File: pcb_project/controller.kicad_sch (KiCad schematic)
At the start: 16 parts, among them U5 COM-09032, U6 COM-09032

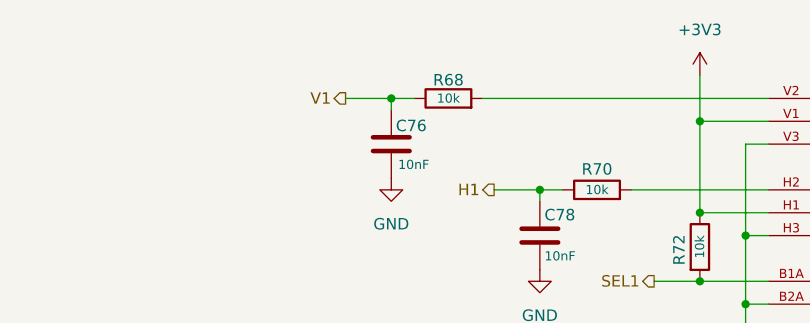
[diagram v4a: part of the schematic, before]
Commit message: Fix USB pins and other ERC errors
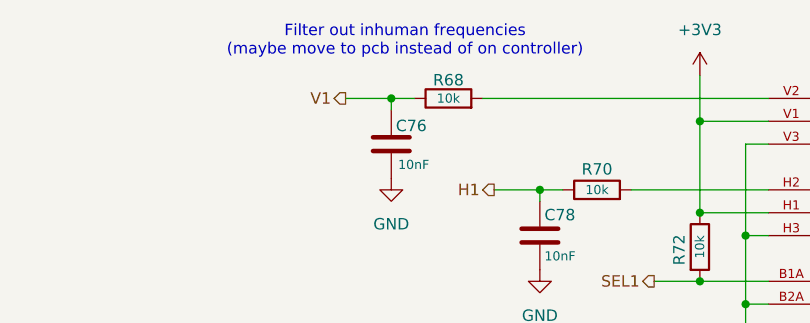
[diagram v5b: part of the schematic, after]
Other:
- note added: "Filter out inhuman frequencies (maybe move to pcb instead of on controller)"
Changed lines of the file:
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@@
 	(generator_version "9.0")
 	(paper "A4")
+	(text "Filter out inhuman frequencies \n(maybe move to pcb instead of on controller)"
+		(exclude_from_sim no)
+		(at 156.464 34.29 0)
+		(effects
+			(font
+				(size 1.27 1.27)
+			)
+		)
+	)
 	(junction
 		(at 194.31 133.35)

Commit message: Add most footprints, missing some inductors and 3 buttons
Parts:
- C76, C77, C78, C79: footprint (none) -> Capacitor_SMD:C_0603_1608Metric_Pad1.08x0.95mm_HandSolder
- R66, R67, R68, R69, R70, R71, R72, R73: footprint (none) -> Resistor_SMD:R_0805_2012Metric_Pad1.20x1.40mm_HandSolder
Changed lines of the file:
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@@
 			)
 		)
-		(property "Footprint" ""
+		(property "Footprint" "Resistor_SMD:R_0805_2012Metric_Pad1.20x1.40mm_HandSolder"
 			(at 177.8 112.268 90)
 			(effects
@@
 			)
 		)
-		(property "Footprint" ""
+		(property "Footprint" "Resistor_SMD:R_0805_2012Metric_Pad1.20x1.40mm_HandSolder"
 			(at 161.29 102.108 90)
 			(effects
@@
 			)
 		)
-		(property "Footprint" ""
+		(property "Footprint" "Resistor_SMD:R_0805_2012Metric_Pad1.20x1.40mm_HandSolder"
 			(at 80.772 55.88 90)
 			(effects
@@
 			)
 		)
-		(property "Footprint" ""
+		(property "Footprint" "Capacitor_SMD:C_0603_1608Metric_Pad1.08x0.95mm_HandSolder"
 			(at 172.4152 119.38 0)
 			(effects
@@
 			)
 		)
-		(property "Footprint" ""
+		(property "Footprint" "Resistor_SMD:R_0805_2012Metric_Pad1.20x1.40mm_HandSolder"
 			(at 187.452 57.15 90)
 			(effects
@@
 			)
 		)
-		(property "Footprint" ""
+		(property "Footprint" "Capacitor_SMD:C_0603_1608Metric_Pad1.08x0.95mm_HandSolder"
 			(at 155.9052 49.53 0)
 			(effects
@@
 			)
 		)
-		(property "Footprint" ""
+		(property "Footprint" "Capacitor_SMD:C_0603_1608Metric_Pad1.08x0.95mm_HandSolder"
 			(at 155.9052 109.22 0)
 			(effects
@@
 			)
 		)
-		(property "Footprint" ""
+		(property "Footprint" "Resistor_SMD:R_0805_2012Metric_Pad1.20x1.40mm_HandSolder"
 			(at 80.772 85.09 90)
 			(effects
@@
 			)
 		)
-		(property "Footprint" ""
+		(property "Footprint" "Capacitor_SMD:C_0603_1608Metric_Pad1.08x0.95mm_HandSolder"
 			(at 172.4152 59.69 0)
 			(effects
@@
 			)
 		)
-		(property "Footprint" ""
+		(property "Footprint" "Resistor_SMD:R_0805_2012Metric_Pad1.20x1.40mm_HandSolder"
 			(at 161.29 42.418 90)
 			(effects
@@
 			)
 		)
-		(property "Footprint" ""
+		(property "Footprint" "Resistor_SMD:R_0805_2012Metric_Pad1.20x1.40mm_HandSolder"
 			(at 187.452 116.84 90)
 			(effects
@@
 			)
 		)
-		(property "Footprint" ""
+		(property "Footprint" "Resistor_SMD:R_0805_2012Metric_Pad1.20x1.40mm_HandSolder"
 			(at 177.8 52.578 90)
 			(effects
